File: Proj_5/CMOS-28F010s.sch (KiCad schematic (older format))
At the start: 8 parts, among them U10 28F010, U11 28F010, U4 28F010, U5 28F010, U6 28F010, U7 28F010, U8 28F010, U9 28F010

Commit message: Labeled Data Bus and Address bus wires in CMOS
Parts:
- added U? (x2): 74LS138, symbol 74xx_IEEE:74LS138
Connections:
- net labels added: A0, A1, A10, A11, A12, A13, A14, A15, A16, A17, A18, A19, A2, A3, A4, A5, A6, A7, A8, A9, BHE\, D0, D1, D2, D3, D4, D5, D6, D7
- wire segments 232 -> 243
- no-connect marks 10 -> 12

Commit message: Added address decoding
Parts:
- gave numbers to parts that had none: 2
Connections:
- wire segments 243 -> 264
- no-connect marks 12 -> 19
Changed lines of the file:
@@
 	3500 7900 3600 8000
 Entry Wire Line
-	3500 8000 3600 8100
-Entry Wire Line
 	3500 8100 3600 8200
 Entry Wire Line
@@
 	3600 8000 4650 8000
 Wire Wire Line
-	3600 8100 4650 8100
-Wire Wire Line
 	3600 8200 4650 8200
 Wire Wire Line
@@
 Wire Wire Line
 	3600 8500 4650 8500
-Wire Wire Line
-	3600 8600 4650 8600
 Wire Wire Line
 	3600 8700 4650 8700
@@
 	3500 3400 3600 3500
 Entry Wire Line
-	3500 3500 3600 3600
-Entry Wire Line
 	3500 3600 3600 3700
 Wire Wire Line
@@
 	3600 3000 4650 3000
 Wire Wire Line
-	3600 3100 4650 3100
-Wire Wire Line
-	3600 3200 4650 3200
-Wire Wire Line
-	3600 3300 4650 3300
-Wire Wire Line
 	3600 3400 4650 3400
 Wire Wire Line
 	3600 3500 4650 3500
-Wire Wire Line
-	3600 3600 4650 3600
-Wire Wire Line
-	3600 3700 4650 3700
 $Comp
 L 28F010:28F010 U4
@@
 	7450 2900 7350 3000
 Entry Wire Line
-	7450 3200 7350 3300
-Entry Wire Line
 	7450 3400 7350 3500
 Wire Wire Line
@@
 	6850 3000 7350 3000
 Wire Wire Line
-	7350 3300 6850 3300
-Wire Wire Line
 	7350 3500 6850 3500
 Entry Wire Line
@@
 Wire Wire Line
 	7350 21000 6850 21000
-NoConn ~ 7450 800
 Text HLabel 3500 850  0    50   Input ~ 0
 AddressBus
@@
 	7450 3000 7350 3100
 Entry Wire Line
-	7450 3100 7350 3200
-Wire Wire Line
-	7350 3100 6850 3100
-Wire Wire Line
-	7350 3200 6850 3200
-Entry Wire Line
 	7450 5700 7350 5800
 Entry Wire Line
@@
 	7350 20700 6850 20700
 $Comp
-L 74xx_IEEE:74LS138 U?
+L 74xx_IEEE:74LS138 U12
 U 1 1 5EA276E4
-P 8700 3100
-F 0 "U?" H 8700 3616 50  0000 C CNN
-F 1 "74LS138" H 8700 3525 50  0000 C CNN
-F 2 "" H 8700 3100 50  0001 C CNN
-F 3 "" H 8700 3100 50  0001 C CNN
-	1    8700 3100
-	1    0    0    -1
+P 9300 2150
+F 0 "U12" H 9300 2666 50  0000 C CNN
+F 1 "74LS138" H 9300 2575 50  0000 C CNN
+F 2 "" H 9300 2150 50  0001 C CNN
+F 3 "" H 9300 2150 50  0001 C CNN
+	1    9300 2150
+	0    1    1    0
 $EndComp
 $Comp
-L 74xx_IEEE:74LS138 U?
+L 74xx_IEEE:74LS138 U13
 U 1 1 5EA24F71
-P 8700 1350
-F 0 "U?" H 8700 1866 50  0000 C CNN
-F 1 "74LS138" H 8700 1775 50  0000 C CNN
-F 2 "" H 8700 1350 50  0001 C CNN
-F 3 "" H 8700 1350 50  0001 C CNN
-	1    8700 1350
-	1    0    0    -1
+P 11050 2150
+F 0 "U13" H 11050 2666 50  0000 C CNN
+F 1 "74LS138" H 11050 2575 50  0000 C CNN
+F 2 "" H 11050 2150 50  0001 C CNN
+F 3 "" H 11050 2150 50  0001 C CNN
+	1    11050 2150
+	0    1    1    0
 $EndComp
 $Comp
-L power:GND #PWR?
+L power:GND #PWR0109
 U 1 1 5EAE3763
-P 8700 3700
-F 0 "#PWR?" H 8700 3450 50  0001 C CNN
-F 1 "GND" H 8705 3527 50  0000 C CNN
-F 2 "" H 8700 3700 50  0001 C CNN
-F 3 "" H 8700 3700 50  0001 C CNN
-	1    8700 3700
-	1    0    0    -1
+P 8700 2150
+F 0 "#PWR0109" H 8700 1900 50  0001 C CNN
+F 1 "GND" H 8705 1977 50  0000 C CNN
+F 2 "" H 8700 2150 50  0001 C CNN
+F 3 "" H 8700 2150 50  0001 C CNN
+	1    8700 2150
+	0    1    1    0
 $EndComp
 $Comp
-L power:GND #PWR?
+L power:GND #PWR0110
 U 1 1 5EAE462A
-P 8700 1950
-F 0 "#PWR?" H 8700 1700 50  0001 C CNN
-F 1 "GND" H 8705 1777 50  0000 C CNN
-F 2 "" H 8700 1950 50  0001 C CNN
-F 3 "" H 8700 1950 50  0001 C CNN
-	1    8700 1950
-	1    0    0    -1
+P 10450 2150
+F 0 "#PWR0110" H 10450 1900 50  0001 C CNN
+F 1 "GND" H 10455 1977 50  0000 C CNN
+F 2 "" H 10450 2150 50  0001 C CNN
+F 3 "" H 10450 2150 50  0001 C CNN
+	1    10450 2150
+	0    1    1    0
 $EndComp
 $Comp
-L power:+5V #PWR?
+L power:+5V #PWR0111
 U 1 1 5EAE587A
-P 8700 2800
-F 0 "#PWR?" H 8700 2650 50  0001 C CNN
-F 1 "+5V" H 8715 2973 50  0000 C CNN
-F 2 "" H 8700 2800 50  0001 C CNN
-F 3 "" H 8700 2800 50  0001 C CNN
-	1    8700 2800
-	1    0    0    -1
+P 9600 2150
+F 0 "#PWR0111" H 9600 2000 50  0001 C CNN
+F 1 "+5V" H 9615 2323 50  0000 C CNN
+F 2 "" H 9600 2150 50  0001 C CNN
+F 3 "" H 9600 2150 50  0001 C CNN
+	1    9600 2150
+	0    1    1    0
 $EndComp
 $Comp
-L power:+5V #PWR?
+L power:+5V #PWR0112
 U 1 1 5EAE76B4
-P 8700 1050
-F 0 "#PWR?" H 8700 900 50  0001 C CNN
-F 1 "+5V" H 8715 1223 50  0000 C CNN
-F 2 "" H 8700 1050 50  0001 C CNN
-F 3 "" H 8700 1050 50  0001 C CNN
-	1    8700 1050
-	1    0    0    -1
-$EndComp
-Entry Wire Line
-	7450 1500 7550 1600
-Entry Wire Line
-	7450 1600 7550 1700
-Entry Wire Line
-	7450 3250 7550 3350
-Entry Wire Line
-	7450 3350 7550 3450
-Wire Wire Line
-	7550 1600 8150 1600
-Wire Wire Line
-	7550 1700 8150 1700
-Wire Wire Line
-	7550 3350 8150 3350
-Wire Wire Line
-	7550 3450 8150 3450
-NoConn ~ 8150 1800
-NoConn ~ 8150 3550
-$Comp
-L power:GND #PWR?
-U 1 1 5EBA5C17
-P 7950 1250
-F 0 "#PWR?" H 7950 1000 50  0001 C CNN
-F 1 "GND" V 7955 1122 50  0000 R CNN
-F 2 "" H 7950 1250 50  0001 C CNN
-F 3 "" H 7950 1250 50  0001 C CNN
-	1    7950 1250
+P 11350 2150
+F 0 "#PWR0112" H 11350 2000 50  0001 C CNN
+F 1 "+5V" H 11365 2323 50  0000 C CNN
+F 2 "" H 11350 2150 50  0001 C CNN
+F 3 "" H 11350 2150 50  0001 C CNN
+	1    11350 2150
 	0    1    1    0
 $EndComp
-Wire Wire Line
-	7950 1250 8150 1250
-Wire Wire Line
-	7950 1250 7950 1150
-Wire Wire Line
-	7950 1150 8150 1150
-Connection ~ 7950 1250
-Entry Wire Line
-	7450 1250 7550 1350
-Wire Wire Line
-	7550 1350 8150 1350
-Text HLabel 8150 3100 0    50   Input ~ 0
+NoConn ~ 10600 1600
+NoConn ~ 8850 1600
+$Comp
+L power:GND #PWR0113
+U 1 1 5EBA5C17
+P 11150 1400
+F 0 "#PWR0113" H 11150 1150 50  0001 C CNN
+F 1 "GND" V 11155 1272 50  0000 R CNN
+F 2 "" H 11150 1400 50  0001 C CNN
+F 3 "" H 11150 1400 50  0001 C CNN
+	1    11150 1400
+	-1   0    0    1
+$EndComp
+Wire Wire Line
+	11150 1400 11150 1600
+Wire Wire Line
+	11150 1400 11250 1400
+Wire Wire Line
+	11250 1400 11250 1600
+Connection ~ 11150 1400
+Text HLabel 9300 1600 1    50   Input ~ 0
 BHE\
 $Comp
-L power:GND #PWR?
+L power:GND #PWR0114
 U 1 1 5EC28A77
-P 7950 3000
-F 0 "#PWR?" H 7950 2750 50  0001 C CNN
-F 1 "GND" V 7955 2872 50  0000 R CNN
-F 2 "" H 7950 3000 50  0001 C CNN
-F 3 "" H 7950 3000 50  0001 C CNN
-	1    7950 3000
-	0    1    1    0
+P 9400 1400
+F 0 "#PWR0114" H 9400 1150 50  0001 C CNN
+F 1 "GND" V 9405 1272 50  0000 R CNN
+F 2 "" H 9400 1400 50  0001 C CNN
+F 3 "" H 9400 1400 50  0001 C CNN
+	1    9400 1400
+	-1   0    0    1
 $EndComp
 Wire Wire Line
-	7950 3000 8150 3000
-Wire Wire Line
-	7950 3000 7950 2900
-Wire Wire Line
-	7950 2900 8150 2900
-Connection ~ 7950 3000
-Text Label 7550 1350 0    50   ~ 0
-A0
-Text Label 7550 1600 0    50   ~ 0
-A1
-Text Label 7550 1700 0    50   ~ 0
-A2
-Text Label 7550 3350 0    50   ~ 0
-A1
-Text Label 7550 3450 0    50   ~ 0
-A2
+	9400 1400 9400 1600
+Wire Wire Line
+	9400 1400 9500 1400
+Wire Wire Line
+	9500 1400 9500 1600
+Connection ~ 9400 1400
 Text Label 7100 3700 0    50   ~ 0
 D7
@@
 Text Label 4300 3700 0    50   ~ 0
 A3
-Text Label 4300 3600 0    50   ~ 0
-A4
 Text Label 4300 3500 0    50   ~ 0
 A5
@@
 Text Label 7100 20400 0    50   ~ 0
 A17
+Entry Wire Line
+	7450 800  7550 900
+Wire Wire Line
+	7550 900  11050 900
+Wire Wire Line
+	11050 900  11050 1600
+Text Label 7550 900  0    50   ~ 0
+A0
+Entry Wire Line
+	7450 900  7550 1000
+Entry Wire Line
+	7450 1000 7550 1100
+Wire Wire Line
+	7550 1000 9050 1000
+Wire Wire Line
+	10800 1000 10800 1600
+Wire Wire Line
+	7550 1100 8950 1100
+Wire Wire Line
+	10700 1100 10700 1600
+Wire Wire Line
+	9050 1000 9050 1600
+Connection ~ 9050 1000
+Wire Wire Line
+	9050 1000 10800 1000
+Wire Wire Line
+	8950 1100 8950 1600
+Connection ~ 8950 1100
+Wire Wire Line
+	8950 1100 10700 1100
+Text Label 7550 1000 0    50   ~ 0
+A1
+Text Label 7550 1100 0    50   ~ 0
+A2
+Wire Wire Line
+	9200 2700 9200 3600
+Wire Wire Line
+	9200 3600 6850 3600
+Wire Wire Line
+	9300 2700 9300 6100
+Wire Wire Line
+	9300 6100 6850 6100
+Wire Wire Line
+	9400 2700 9400 8600
+Wire Wire Line
+	9400 8600 6850 8600
+Wire Wire Line
+	9500 2700 9500 11100
+Wire Wire Line
+	9500 11100 6850 11100
+Wire Wire Line
+	10950 2700 10950 13600
+Wire Wire Line
+	10950 13600 6850 13600
+Wire Wire Line
+	11050 2700 11050 16100
+Wire Wire Line
+	11050 16100 6850 16100
+Wire Wire Line
+	11150 2700 11150 18650
+Wire Wire Line
+	11150 18650 6850 18650
+Wire Wire Line
+	11250 2700 11250 21100
+Wire Wire Line
+	11250 21100 6850 21100
+NoConn ~ 8800 2700
+NoConn ~ 8900 2700
+NoConn ~ 9000 2700
+NoConn ~ 9100 2700
+NoConn ~ 10550 2700
+NoConn ~ 10650 2700
+NoConn ~ 10750 2700
+NoConn ~ 10850 2700
+Entry Wire Line
+	3500 3500 3600 3600
+Wire Wire Line
+	3600 3600 4650 3600
+Text Label 4300 3600 0    50   ~ 0
+A4
+Wire Wire Line
+	3600 3300 4650 3300
+Wire Wire Line
+	4650 3100 3600 3100
+Wire Wire Line
+	4650 3200 3600 3200
+Wire Wire Line
+	3600 3700 4650 3700
+Wire Wire Line
+	7350 3100 6850 3100
+Entry Wire Line
+	7450 3100 7350 3200
+Entry Wire Line
+	7450 3200 7350 3300
+Wire Wire Line
+	7350 3200 6850 3200
+Wire Wire Line
+	7350 3300 6850 3300
+Wire Wire Line
+	3600 8600 4650 8600
+Wire Wire Line
+	4650 8100 3600 8100
+Entry Wire Line
+	3500 8000 3600 8100
 Wire Bus Line
 	2850 850  2850 4500

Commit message: Added some connections; Some connections are reporting 'No connections' and IDK why
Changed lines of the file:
@@
 Comment4 ""
 $EndDescr
-Text Notes 3400 13850 1    256  ~ 0
+Text Notes 11750 2500 3    256  ~ 0
 Low Bank\n
-Text Notes 3350 2850 1    256  ~ 0
+Text Notes 10000 2500 3    256  ~ 0
 High Bank
 Entry Wire Line

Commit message: Fixed CMOS and connected to processor. Still missing some pins though
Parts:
- removed U10, U11, U5, U6, U7, U8, U9: 28F010, 28F010, symbol 28F010:28F010
- removed U12, U13: 74LS138, symbol 74xx_IEEE:74LS138
- added U5: 74LVC1G10, symbol 74xGxx:74LVC1G10
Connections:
- net labels added: VCC, ~OE, ~WE
- net labels removed: +5V, AddressBus, BHE\, DataBus
- wire segments 264 -> 41
- no-connect marks 19 -> 1
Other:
- note removed: "High Bank"
- note removed: "Low Bank\n"

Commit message: Please dont break
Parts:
- removed U5: 74LVC1G10, symbol 74xGxx:74LVC1G10
- added U?: 28F010, 28F010, symbol 28F010:28F010
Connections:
- net labels added: D10, D11, D12, D13, D14, D15, D8, D9, WE, ~BHE, ~BLE
- net labels removed: A0, A1, A2, ~WE
- wire segments 41 -> 68
- no-connect marks 1 -> 2
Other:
- note added: "High Bank"
- note added: "Low Bank"
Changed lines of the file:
@@
 	7350 2900 6850 2900
-Wire Wire Line
-	6850 3000 7350 3000
 Wire Wire Line
 	7350 3500 6850 3500
@@
 Wire Wire Line
 	7350 3300 6850 3300
-Wire Wire Line
-	6850 3600 7750 3600
-Wire Wire Line
-	7750 3600 7750 2800
-Wire Wire Line
-	7550 2000 7850 2000
-Wire Wire Line
-	7850 2000 7850 2200
-Wire Wire Line
-	7550 2100 7750 2100
-Wire Wire Line
-	7750 2100 7750 2200
-Wire Wire Line
-	7550 2200 7650 2200
-$Comp
-L 74xGxx:74LVC1G10 U5
-U 1 1 5EB89412
-P 7750 2500
-F 0 "U5" V 7704 2677 50  0000 L CNN
-F 1 "74LVC1G10" V 7795 2677 50  0000 L CNN
-F 2 "" H 7750 2500 50  0001 C CNN
-F 3 "http://www.ti.com/lit/sg/scyt129e/scyt129e.pdf" H 7750 2500 50  0001 C CNN
-	1    7750 2500
-	0    1    1    0
-$EndComp
 Text HLabel 3600 3700 0    50   Input ~ 0
 A3
@@
 Text HLabel 7350 3500 2    50   Input ~ 0
 A13
-Text HLabel 7550 2000 0    50   Input ~ 0
-A0
-Text HLabel 7550 2100 0    50   Input ~ 0
-A1
-Text HLabel 7550 2200 0    50   Input ~ 0
-A2
 Text HLabel 7250 3700 2    50   BiDi ~ 0
-D7
+D15
 Text HLabel 7250 3800 2    50   BiDi ~ 0
-D6
+D14
 Text HLabel 7250 3900 2    50   BiDi ~ 0
-D5
+D13
 Text HLabel 7250 4000 2    50   BiDi ~ 0
-D4
+D12
 Text HLabel 7250 4100 2    50   BiDi ~ 0
-D3
+D11
 Text HLabel 2950 3800 0    50   BiDi ~ 0
-D0
+D8
 Text HLabel 2950 3900 0    50   BiDi ~ 0
-D1
+D9
 Text HLabel 2950 4000 0    50   BiDi ~ 0
-D2
-Text HLabel 6850 2700 2    50   Input ~ 0
-~WE
+D10
 Wire Wire Line
 	3600 3700 4650 3700
-Text HLabel 6850 3400 2    50   Input ~ 0
-~OE
 $Comp
 L power:VCC #PWR0107
@@
 Wire Wire Line
 	7000 2050 7000 2150
+Wire Wire Line
+	3600 5400 4650 5400
+Wire Wire Line
+	3600 5500 4650 5500
+Wire Wire Line
+	3600 5600 4650 5600
+Wire Wire Line
+	3600 5700 4650 5700
+Wire Wire Line
+	3600 6100 4650 6100
+Wire Wire Line
+	3600 6200 4650 6200
+$Comp
+L 28F010:28F010 U?
+U 1 1 5EA1E756
+P 4650 5300
+F 0 "U?" H 5750 5687 60  0000 C CNN
+F 1 "28F010" H 5750 5581 60  0000 C CNN
+F 2 "28F010" H 5750 5540 60  0001 C CNN
+F 3 "" H 4650 5300 60  0000 C CNN
+	1    4650 5300
+	1    0    0    -1
+$EndComp
+Wire Wire Line
+	7350 5600 6850 5600
+Wire Wire Line
+	6850 5700 7350 5700
+Wire Wire Line
+	7350 6200 6850 6200
+Wire Wire Line
+	7250 6500 6850 6500
+Wire Wire Line
+	7250 6600 6850 6600
+Wire Wire Line
+	7250 6700 6850 6700
+Wire Wire Line
+	7250 6800 6850 6800
+Wire Wire Line
+	7250 6400 6850 6400
+Wire Wire Line
+	2950 6500 4650 6500
+Wire Wire Line
+	2950 6600 4650 6600
+Wire Wire Line
+	2950 6700 4650 6700
+Wire Wire Line
+	6850 5300 7000 5300
+Wire Wire Line
+	4500 6800 4650 6800
+NoConn ~ 6850 5500
+Wire Wire Line
+	3600 6300 4650 6300
+Wire Wire Line
+	3600 6000 4650 6000
+Wire Wire Line
+	4650 5800 3600 5800
+Wire Wire Line
+	4650 5900 3600 5900
+Wire Wire Line
+	7350 5800 6850 5800
+Wire Wire Line
+	7350 5900 6850 5900
+Wire Wire Line
+	7350 6000 6850 6000
+Text HLabel 3600 6400 0    50   Input ~ 0
+A3
+Text HLabel 3600 6300 0    50   Input ~ 0
+A4
+Text HLabel 3600 6200 0    50   Input ~ 0
+A5
+Text HLabel 3600 6100 0    50   Input ~ 0
+A6
+Text HLabel 3600 6000 0    50   Input ~ 0
+A7
+Text HLabel 3600 5900 0    50   Input ~ 0
+A8
+Text HLabel 3600 5800 0    50   Input ~ 0
+A9
+Text HLabel 3600 5700 0    50   Input ~ 0
+A10
+Text HLabel 3600 5600 0    50   Input ~ 0
+A15
+Text HLabel 3600 5500 0    50   Input ~ 0
+A18
+Text HLabel 3600 5400 0    50   Input ~ 0
+A19
+Text HLabel 7350 5600 2    50   Input ~ 0
+A17
+Text HLabel 7350 5700 2    50   Input ~ 0
+A16
+Text HLabel 7350 5800 2    50   Input ~ 0
+A11
+Text HLabel 7350 5900 2    50   Input ~ 0
+A12
+Text HLabel 7350 6000 2    50   Input ~ 0
+A14
+Text HLabel 7350 6200 2    50   Input ~ 0
+A13
+Text HLabel 7250 6400 2    50   BiDi ~ 0
+D7
+Text HLabel 7250 6500 2    50   BiDi ~ 0
+D6
+Text HLabel 7250 6600 2    50   BiDi ~ 0
+D5
+Text HLabel 7250 6700 2    50   BiDi ~ 0
+D4
+Text HLabel 7250 6800 2    50   BiDi ~ 0
+D3
+Text HLabel 2950 6500 0    50   BiDi ~ 0
+D0
+Text HLabel 2950 6600 0    50   BiDi ~ 0
+D1
+Text HLabel 2950 6700 0    50   BiDi ~ 0
+D2
+Wire Wire Line
+	3600 6400 4650 6400
+Wire Wire Line
+	7000 4850 4650 4850
+Wire Wire Line
+	4650 4850 4650 5300
+Connection ~ 7000 4850
+Wire Wire Line
+	7000 4850 7000 5300
+Wire Wire Line
+	7000 2600 7000 4850
+Connection ~ 7000 2600
+Wire Wire Line
+	7350 2700 6850 2700
+Wire Wire Line
+	6850 5400 7450 5400
+Wire Wire Line
+	4500 4100 4500 6800
+Connection ~ 4500 4100
+Wire Wire Line
+	7350 3000 6850 3000
+Text HLabel 6850 6300 2    50   Input ~ 0
+~BLE
+Text Notes 7950 3200 0    197  ~ 0
+High Bank
+Text Notes 7950 5700 0    197  ~ 0
+Low Bank
+Text HLabel 7350 2700 2    50   Input ~ 0
+WE
+Text HLabel 7450 5400 2    50   Input ~ 0
+WE
+Text HLabel 6850 3600 2    50   Input ~ 0
+~BHE
+Text HLabel 6850 3400 2    50   Input ~ 0
+~OE
+Text HLabel 6850 6100 2    50   Input ~ 0
+~OE
 $EndSCHEMATC

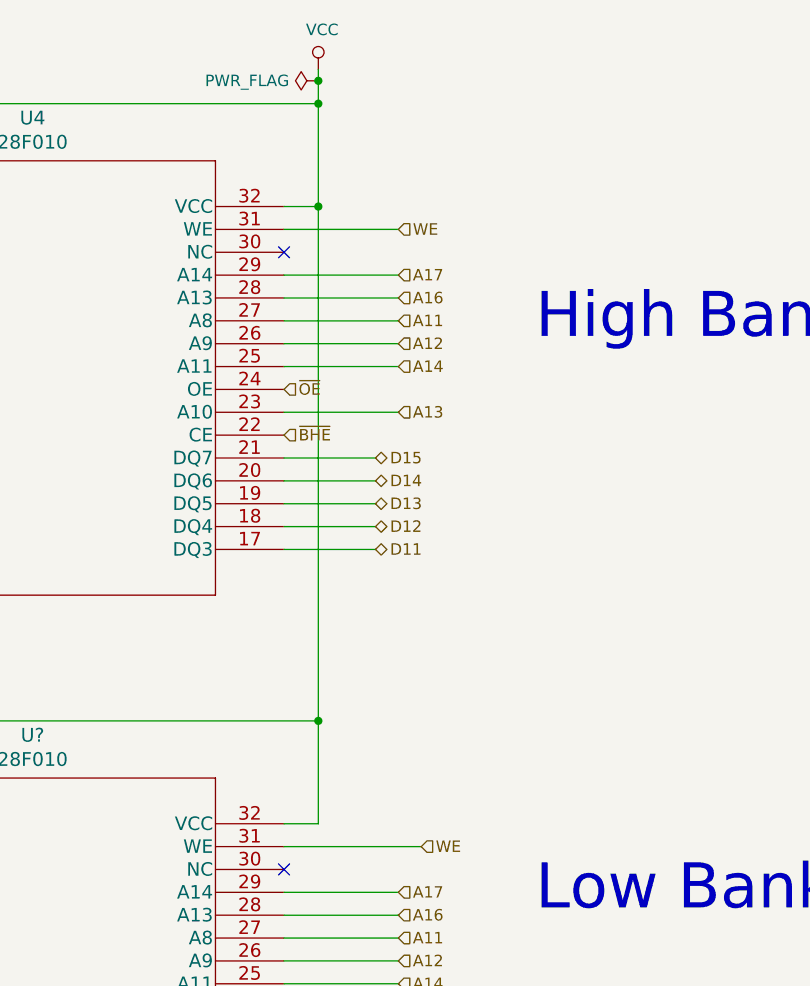
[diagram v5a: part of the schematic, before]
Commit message: Added Caps to Each Vcc per desc.
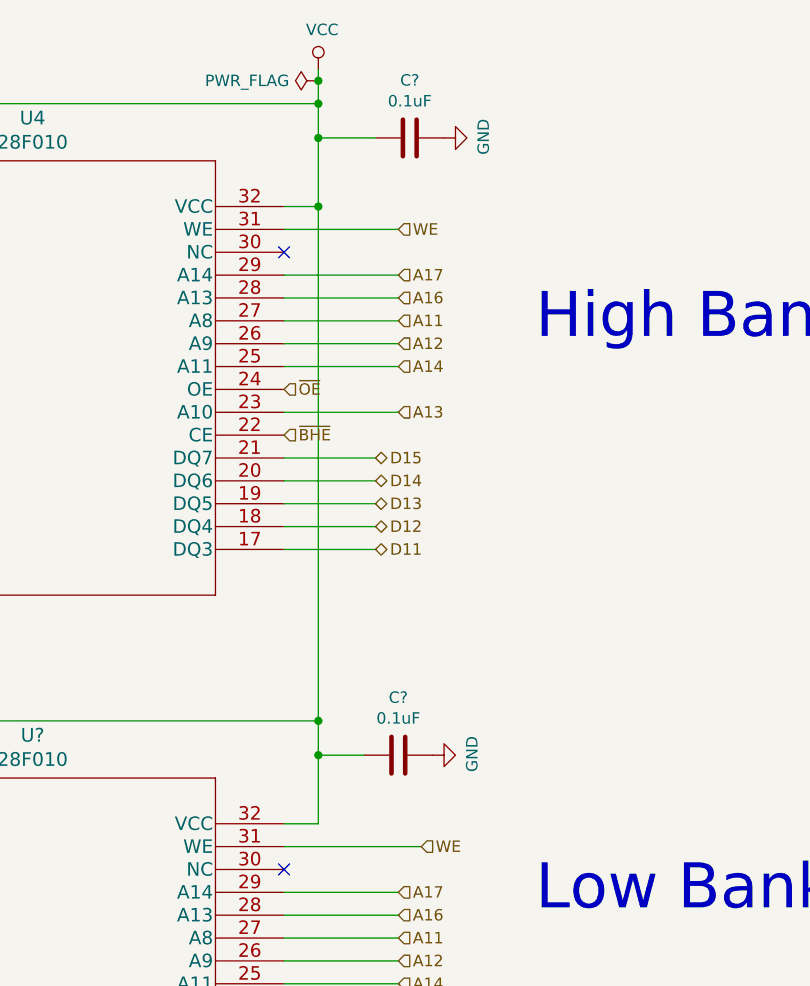
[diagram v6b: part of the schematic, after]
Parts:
- added C? (x2): 0.1uF, symbol Device:C
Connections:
- net GND: now also C?.1, C?.1
- net VCC: now also C?.2, C?.2
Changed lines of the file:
@@
 Connection ~ 7000 2150
 Wire Wire Line
-	7000 2150 7000 2600
+	7000 2150 7000 2300
 Connection ~ 7000 2050
 Wire Wire Line
@@
 Connection ~ 7000 4850
 Wire Wire Line
-	7000 4850 7000 5300
+	7000 4850 7000 5000
 Wire Wire Line
 	7000 2600 7000 4850
@@
 Text HLabel 6850 6100 2    50   Input ~ 0
 ~OE
+$Comp
+L Device:C C?
+U 1 1 5EA60943
+P 7400 2300
+AR Path="/5EA98353/5EA60943" Ref="C?"  Part="1"
+AR Path="/5EA045EA/5EA60943" Ref="C?"  Part="1"
+F 0 "C?" V 7148 2300 50  0000 C CNN
+F 1 "0.1uF" V 7239 2300 50  0000 C CNN
+F 2 "" H 7438 2150 50  0001 C CNN
+F 3 "~" H 7400 2300 50  0001 C CNN
+	1    7400 2300
+	0    1    1    0
+$EndComp
+$Comp
+L Device:C C?
+U 1 1 5EA62C10
+P 7350 5000
+AR Path="/5EA98353/5EA62C10" Ref="C?"  Part="1"
+AR Path="/5EA045EA/5EA62C10" Ref="C?"  Part="1"
+F 0 "C?" V 7098 5000 50  0000 C CNN
+F 1 "0.1uF" V 7189 5000 50  0000 C CNN
+F 2 "" H 7388 4850 50  0001 C CNN
+F 3 "~" H 7350 5000 50  0001 C CNN
+	1    7350 5000
+	0    1    1    0
+$EndComp
+Wire Wire Line
+	7200 5000 7000 5000
+Connection ~ 7000 5000
+Wire Wire Line
+	7000 5000 7000 5300
+Wire Wire Line
+	7250 2300 7000 2300
+Connection ~ 7000 2300
+Wire Wire Line
+	7000 2300 7000 2600
+$Comp
+L power:GND #PWR?
+U 1 1 5EADCED2
+P 7550 2300
+F 0 "#PWR?" H 7550 2050 50  0001 C CNN
+F 1 "GND" H 7555 2127 50  0000 C CNN
+F 2 "" H 7550 2300 50  0001 C CNN
+F 3 "" H 7550 2300 50  0001 C CNN
+	1    7550 2300
+	0    -1   -1   0
+$EndComp
+$Comp
+L power:GND #PWR?
+U 1 1 5EADF0AF
+P 7500 5000
+F 0 "#PWR?" H 7500 4750 50  0001 C CNN
+F 1 "GND" H 7505 4827 50  0000 C CNN
+F 2 "" H 7500 5000 50  0001 C CNN
+F 3 "" H 7500 5000 50  0001 C CNN
+	1    7500 5000
+	0    -1   -1   0
+$EndComp
 $EndSCHEMATC
